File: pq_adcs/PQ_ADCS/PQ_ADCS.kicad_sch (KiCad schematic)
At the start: 55 parts, among them J1 CES-110-02-L-S, J10 Pico-Clasp_01x09, J11 Pico-Clasp_01x15, J12 CES-102-02-L-S, J2 CES-110-02-L-S, J3 CES-110-02-L-S, J4 CES-110-02-L-S, J5 Pico-Clasp_01x02, J6 Pico-Clasp_01x10, J7 Pico-Clasp_01x10, J8 Pico-Clasp_01x10, J9 Pico-Clasp_01x10, U1 LPV542, U2 LPV542, U3 LPV542, U4 IIM-42652, U5 TLC59208FIRGYR, U6 TMUX1108RSVR, U7 TCN75AVOA713

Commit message: designs updated
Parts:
- removed R13, R14: 5k, Resistor_SMD:R_0603_1608Metric, symbol Device:R
- removed U5: TLC59208FIRGYR, symbol SamacSys_Parts:TLC59208FIRGYR
- added C13, C14: 1 uF, Capacitor_SMD:C_0603_1608Metric, symbol Device:C
- added U5: BD2606MVV, Package_DFN_QFN:QFN-16-1EP_4x4mm_P0.65mm_EP2.5x2.5mm, symbol GGS_Miscellaneous:BD2606MVV
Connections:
- net SCL is gone; now on net SCL3: J10.5 (Pin_5), J11.7 (Pin_7), J6.7 (Pin_7), J7.7 (Pin_7), J8.7 (Pin_7), J9.7 (Pin_7), U7.2 (SCL)
- net SDA is gone; now on net SDA3: J10.4 (Pin_4), J11.6 (Pin_6), J6.6 (Pin_6), J7.6 (Pin_6), J8.6 (Pin_6), J9.6 (Pin_6), U7.1 (SDA)
- net VCC is gone; now on net 3V3_PERM: J10.3 (Pin_3), J11.5 (Pin_5), J6.5 (Pin_5), J7.5 (Pin_5), J8.5 (Pin_5), J9.5 (Pin_5)
- net V_UMBILICAL is gone; now on net VCC_UMBILICAL: J11.15 (Pin_15)
- net ADCS_POWER: now also U5.6 (IN); no longer J12.2 (Pin_2)
- net GND: now also U5.11 (GND), U5.17 (EPAD)
- net MAG+X: now also U5.16 (LEDA2)
- net MAG+Y: now also U5.12 (LEDC2)
- net MAG+Z: now also U5.14 (LEDB2)
- net MAG-X: now also U5.1 (LEDA1)
- net MAG-Y: now also U5.13 (LEDC1)
- net MAG-Z: now also U5.15 (LEDB1)
- net SCL3: now also U5.3 (SCL)
- net SDA3: now also U5.2 (SDA)
- net UART_TX: no longer J1.3 (Pin_3)
- net TEMP_A2: now reaches R19.1, R20.2, U7.5 (A2)
- net TEMP_A1: now reaches R17.1, R18.2, U7.6 (A1)
- net TEMP_A0: now reaches R15.1, R16.2, U7.7 (A0)
- new net: C13.1, U5.10 (C2P)
- new net: C13.2, U5.9 (C2N)
- new net: C14.1, U5.8 (C1P)
- new net: C14.2, U5.7 (C1N)
- new net UART_RX: J1.3 (Pin_3)
- new net VCC_MAG: J12.2 (Pin_2), U5.5 (OUT)
- no-connect marks 3 -> 1
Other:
- note added: "I2C address: 1100110"
- note removed: "I2C address: 0000111"
- note removed: "To DO: Change MTQ drivers"
- moved on the sheet: C10, C7, C8, C9, J12, J5, U4, U6

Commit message: lots of changes
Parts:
- removed J5: Pico-Clasp_01x02, Connector_Molex:Molex_Pico-Clasp_202396-0207_1x02-1MP_P1.00mm_Horizontal, symbol Connector_Generic_MountingPin:Conn_01x02_MountingPin
- added J5: Conn_01x03_MountingPin, symbol Connector_Generic_MountingPin:Conn_01x03_MountingPin
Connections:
- net HEATER_EN is gone; now on net GND: J2.7 (Pin_7)
- net 3V3_PERM: now also J10.4 (Pin_4), J11.4 (Pin_4), J6.4 (Pin_4), J7.4 (Pin_4), J8.4 (Pin_4), J9.4 (Pin_4); no longer J10.3 (Pin_3), J11.5 (Pin_5), J6.5 (Pin_5), J7.5 (Pin_5), J8.5 (Pin_5), J9.5 (Pin_5)
- net BATT_NTC: now also J5.1 (Pin_1)
- net BURNCOMMS: now also J10.9 (Pin_9), J6.9 (Pin_9), J7.9 (Pin_9), J8.9 (Pin_9), J9.9 (Pin_9); no longer J10.8 (Pin_8), J6.10 (Pin_10), J7.10 (Pin_10), J8.10 (Pin_10), J9.10 (Pin_10)
- net GND: now also J10.3 (Pin_3), J11.7 (Pin_7), J6.10 (Pin_10), J6.7 (Pin_7), J7.10 (Pin_10), J7.7 (Pin_7), J8.10 (Pin_10), J8.7 (Pin_7), J9.10 (Pin_10), J9.7 (Pin_7), J5.2 (Pin_2), J5.MP (MountPin); no longer J10.9 (Pin_9), J11.2 (Pin_2), J11.4 (Pin_4), J6.2 (Pin_2), J6.4 (Pin_4), J6.9 (Pin_9), J7.2 (Pin_2), J7.4 (Pin_4), J7.9 (Pin_9), J8.2 (Pin_2), J8.4 (Pin_4), J8.9 (Pin_9), J9.2 (Pin_2), J9.4 (Pin_4), J9.9 (Pin_9)
- net HEATER_PWR: now also J5.3 (Pin_3)
- net MAG+X: now also J7.2 (Pin_2); no longer J7.3 (Pin_3)
- net MAG+Y: now also J12.2 (Pin_2); no longer J12.1 (Pin_1)
- net MAG+Z: now also J9.2 (Pin_2); no longer J9.3 (Pin_3)
- net MAG-X: now also J6.2 (Pin_2); no longer J6.3 (Pin_3)
- net MAG-Y: now also J11.2 (Pin_2); no longer J11.3 (Pin_3)
- net MAG-Z: now also J8.2 (Pin_2); no longer J8.3 (Pin_3)
- net PHT6: now also J10.8 (Pin_8); no longer J10.6 (Pin_6)
- net SCL3: now also J10.6 (Pin_6), J11.6 (Pin_6), J6.6 (Pin_6), J7.6 (Pin_6), J8.6 (Pin_6), J9.6 (Pin_6); no longer J10.5 (Pin_5), J11.7 (Pin_7), J6.7 (Pin_7), J7.7 (Pin_7), J8.7 (Pin_7), J9.7 (Pin_7)
- net SDA3: now also J10.5 (Pin_5), J11.5 (Pin_5), J6.5 (Pin_5), J7.5 (Pin_5), J8.5 (Pin_5), J9.5 (Pin_5); no longer J10.4 (Pin_4), J11.6 (Pin_6), J6.6 (Pin_6), J7.6 (Pin_6), J8.6 (Pin_6), J9.6 (Pin_6)
- net VCC_MAG: now also J11.3 (Pin_3), J12.1 (Pin_1), J6.3 (Pin_3), J7.3 (Pin_3), J8.3 (Pin_3), J9.3 (Pin_3); no longer J12.2 (Pin_2)
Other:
- note added: "I2C address:"
- note removed: "I2C address: 1100110"
- moved on the sheet: J10, J11, J12, J8, J9

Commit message: adcs board ready for manufacturing
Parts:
- J5: footprint (none) -> Connector_Molex:Molex_Pico-Clasp_202396-0307_1x03-1MP_P1.00mm_Horizontal
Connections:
- net BATT-: now also J11.10 (Pin_10); no longer J11.11 (Pin_11)
- net KILLSWITCH+: now also J11.11 (Pin_11); no longer J11.10 (Pin_10)
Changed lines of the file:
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@@
+    )
+  )
+  (global_label "BATT-" (shape input) (at 264.16 214.63 0) (fields_autoplaced)
+    (effects (font (size 1.27 1.27)) (justify left))
+    (property "Intersheet References" "${INTERSHEET_REFS}" (id 0) (at 272.4393 214.5506 0)
+      (effects (font (size 1.27 1.27)) (justify left) hide)
     )
   )
@@
     )
   )
-  (global_label "BATT-" (shape input) (at 264.16 217.17 0) (fields_autoplaced)
-    (effects (font (size 1.27 1.27)) (justify left))
-    (property "Intersheet References" "${INTERSHEET_REFS}" (id 0) (at 272.4393 217.0906 0)
-      (effects (font (size 1.27 1.27)) (justify left) hide)
-    )
-  )
   (global_label "SDA3" (shape input) (at 264.16 201.93 0) (fields_autoplaced)
     (effects (font (size 1.27 1.27)) (justify left))
@@
     )
   )
+  (global_label "KILLSWITCH+" (shape input) (at 264.16 217.17 0) (fields_autoplaced)
+    (effects (font (size 1.27 1.27)) (justify left))
+    (property "Intersheet References" "${INTERSHEET_REFS}" (id 0) (at 278.9102 217.0906 0)
+      (effects (font (size 1.27 1.27)) (justify left) hide)
+    )
+  )
   (global_label "GND" (shape input) (at 104.14 252.73 90) (fields_autoplaced)
     (effects (font (size 1.27 1.27)) (justify left))
@@
     (effects (font (size 1.27 1.27)) (justify left))
     (property "Intersheet References" "${INTERSHEET_REFS}" (id 0) (at 71.0406 233.5045 90)
-      (effects (font (size 1.27 1.27)) (justify left) hide)
-    )
-  )
-  (global_label "KILLSWITCH+" (shape input) (at 264.16 214.63 0) (fields_autoplaced)
-    (effects (font (size 1.27 1.27)) (justify left))
-    (property "Intersheet References" "${INTERSHEET_REFS}" (id 0) (at 278.9102 214.5506 0)
       (effects (font (size 1.27 1.27)) (justify left) hide)
     )
@@
       (effects (font (size 1.27 1.27)) hide)
     )
-    (property "Footprint" "" (id 2) (at 321.31 194.31 0)
-      (effects (font (size 1.27 1.27)) hide)
-    )
+    (property "Footprint" "Connector_Molex:Molex_Pico-Clasp_202396-0307_1x03-1MP_P1.00mm_Horizontal" (id 2) (at 321.31 194.31 0)
+      (effects (font (size 1.27 1.27)) hide)
+    )

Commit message: BoM
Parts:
- C1, C2, C3, C4, C5, C6: Manufacturer 1 (none) -> KYOCERA AVX; Manufacturer Part Number 1 (none) -> 06035C101K4T2A; Supplier 1 (none) -> Mouser; Supplier Part Number 1 (none) -> 581-06035C101K4T2A
- J5: value Conn_01x03_MountingPin -> Pico-Clasp_01x03; Manufacturer 1 (none) -> Molex; Manufacturer Part Number 1 (none) -> 203556-0307; Supplier 1 (none) -> Mouser; Supplier Part Number 1 (none) -> 538-203556-0307
- R1, R10, R2, R5, R6, R9: Manufacturer 1 (none) -> YAGEO; Manufacturer Part Number 1 (none) -> AC0603FR-13100RL; Supplier 1 (none) -> Mouser; Supplier Part Number 1 (none) -> 603-AC0603FR-13100RL
- R11, R12, R3, R4, R7, R8: Manufacturer 1 (none) -> YAGEO; Manufacturer Part Number 1 (none) -> RC0603FR-132KL; Supplier 1 (none) -> Mouser; Supplier Part Number 1 (none) -> 603-RC0603FR-132KL
- R15, R16, R17, R18, R19, R20: Manufacturer 1 (none) -> Bourns; Manufacturer Part Number 1 (none) -> CR0402AJ/-000GAS; Supplier 1 (none) -> Mouser; Supplier Part Number 1 (none) -> 652-CR0402AJ/-000GAS
- U5: Manufacturer 1 (none) -> ROHM Semiconductor; Manufacturer Part Number 1 (none) -> BD2606MVV-E2; Supplier 1 (none) -> Mouser; Supplier Part Number 1 (none) -> 755-BD2606MVV-E2

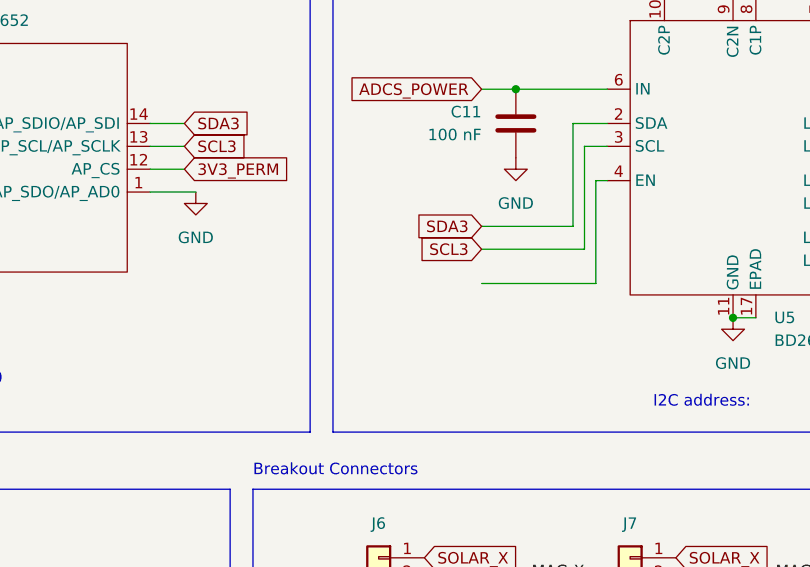
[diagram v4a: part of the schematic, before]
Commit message: MTQ driver's enable connected to VCC_ADCS
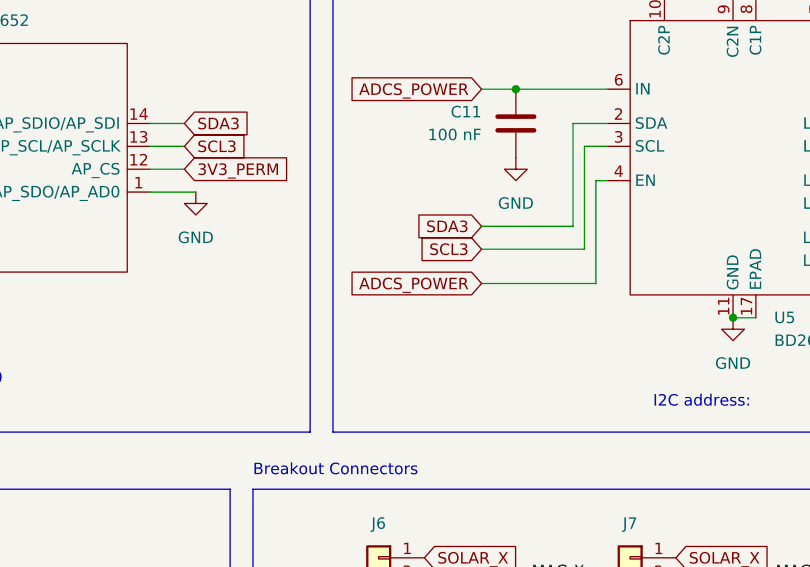
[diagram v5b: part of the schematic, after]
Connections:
- net ADCS_POWER: now also U5.4 (EN)
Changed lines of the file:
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@@
+    )
+  )
+  (global_label "ADCS_POWER" (shape input) (at 151.13 161.29 180) (fields_autoplaced)
+    (effects (font (size 1.27 1.27)) (justify right))
+    (property "Intersheet References" "${INTERSHEET_REFS}" (id 0) (at 136.4402 161.2106 0)
+      (effects (font (size 1.27 1.27)) (justify right) hide)
     )
   )
